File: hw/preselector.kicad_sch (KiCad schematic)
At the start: 51 parts, among them U402 AS169-73LF, U404 AS169-73LF, U406 MCP23S17_SS, U408 AS169-73LF, U412 AS169-73LF, U413 AS169-73LF, U414 AS169-73LF, U415 AS169-73LF, U416 AS169-73LF, U418 AS169-73LF, U419 AS169-73LF, U420 AS169-73LF, U421 AS169-73LF, U422 AS169-73LF, U423 AS169-73LF, U424 AS169-73LF

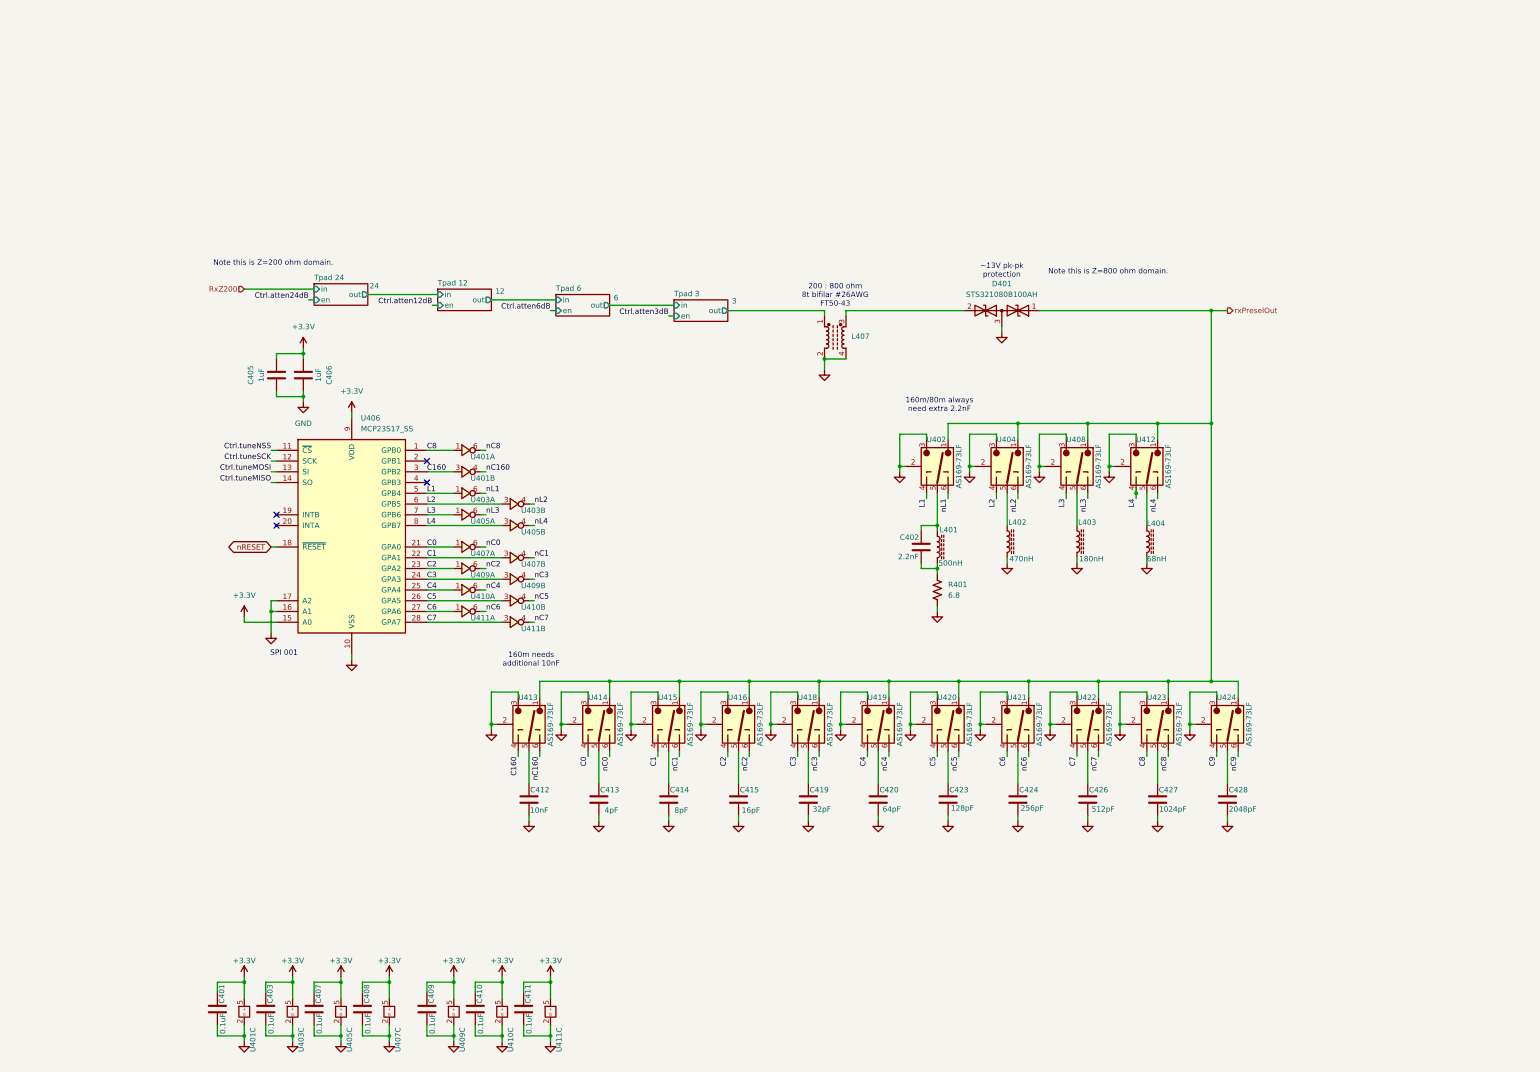
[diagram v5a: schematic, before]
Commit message: USB-PD now "done". Veer power cleaned up a bit. Working voltage increased for caps that need it. Power sequencing for FPGA handled. Analog rails now come from separate buck + (quiet) LDO for each. Starting on digital antenna tuner design.
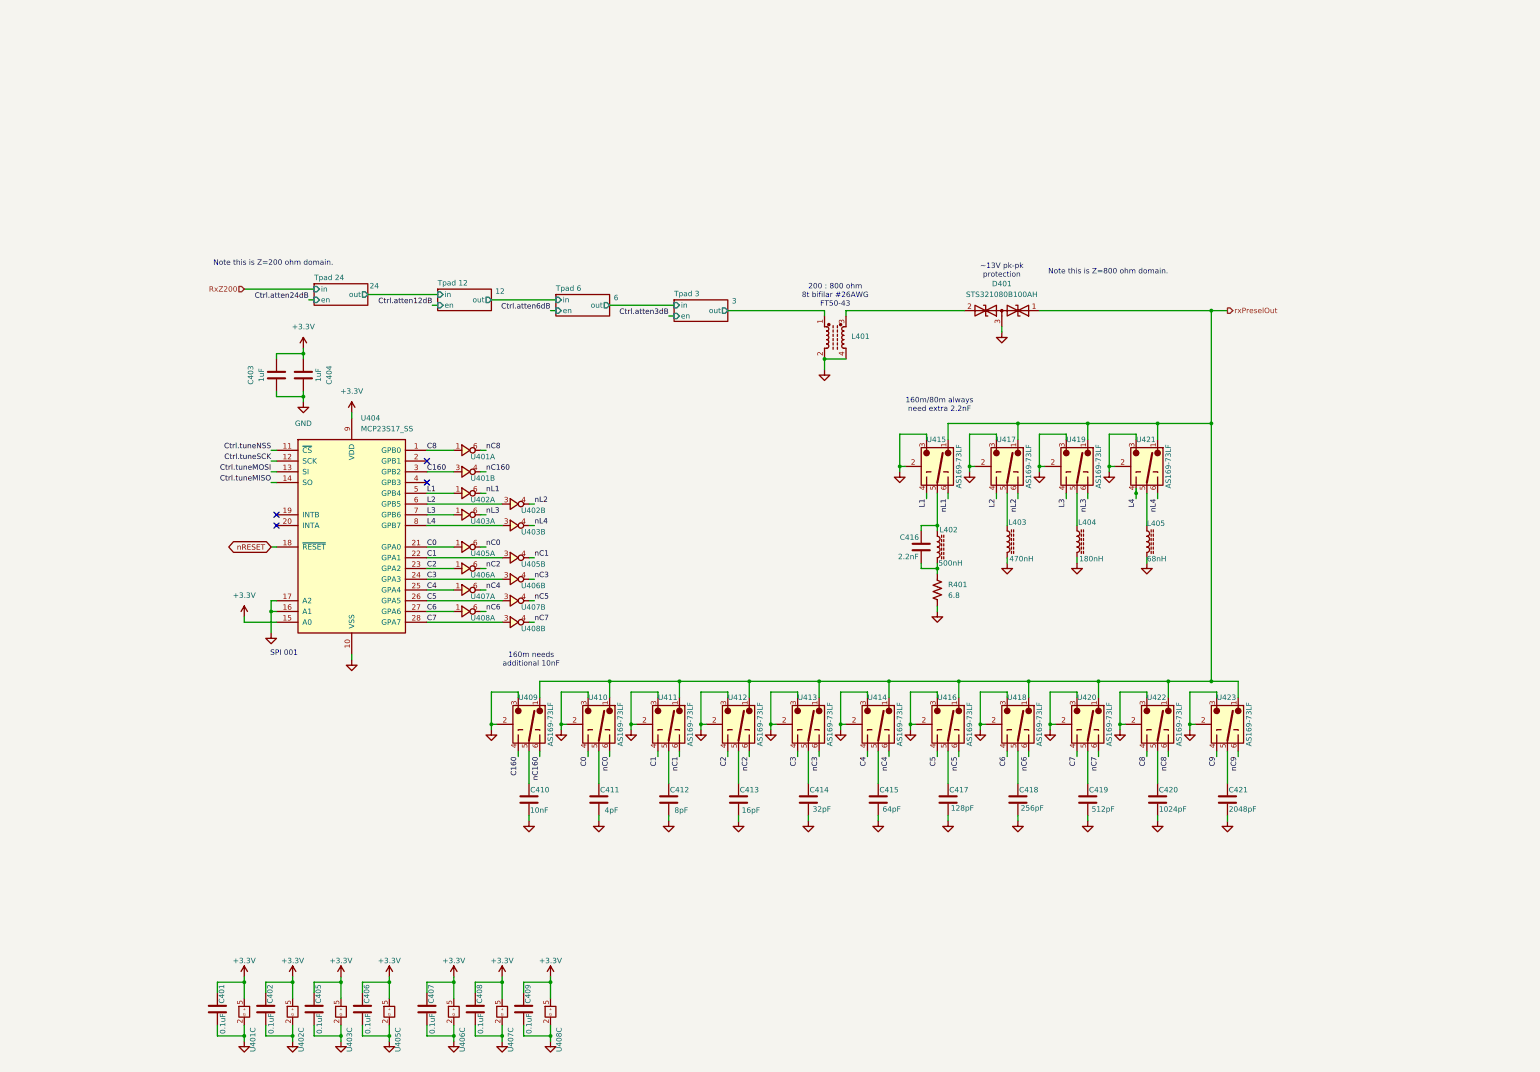
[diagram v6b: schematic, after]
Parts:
- renumbered C403 to C402, C405 to C403, C406 to C404, C407 to C405, C408 to C406, C409 to C407, C410 to C408, C411 to C409, C412 to C410, C413 to C411, C414 to C412, C415 to C413, C419 to C414, C420 to C415, C402 to C416, C423 to C417, C424 to C418, C426 to C419, C427 to C420, C428 to C421, L407 to L401, L401 to L402, L402 to L403, L403 to L404, L404 to L405, U403 to U402, U405 to U403, U406 to U404, U407 to U405, U409 to U406, U410 to U407, U411 to U408, U413 to U409, U414 to U410, U415 to U411, U416 to U412, U418 to U413, U419 to U414, U402 to U415, U420 to U416, U404 to U417, U421 to U418, U408 to U419, U422 to U420, U412 to U421, U423 to U422, U424 to U423

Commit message: Ready for first schematic review with Claude.ai
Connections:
- net Ctrl.tuneMISO renamed Ctrl.tuneRCK
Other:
- company: (none) -> WB7NAB
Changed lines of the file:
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@@
 		(title "Receive Preselector")
 		(date "2025-10-13")
+		(company "WB7NAB")
+		(comment 1 "Alan Mimms")
 	)
 	(text "SPI 001"
@@
 		)
 	)
-	(label "Ctrl.tuneMISO"
+	(label "Ctrl.tuneRCK"
 		(at 27.94 64.77 180)
 		(effects

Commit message: After Claude schematic review all issues resolved.
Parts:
- removed D401: STS321080B100AH, Diode_SMD:D_SOD-323, symbol Diode:SM712_SOT23
- U409, U410, U411, U412, U413, U414, U415, U416, U417, U418, U419, U420, U421, U422, U423: value AS169-73LF -> AS183-92LF
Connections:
- net rxPreselOut: now also L401.3
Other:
- note removed: "~13V pk-pk protection"
- moved on the sheet: L401
